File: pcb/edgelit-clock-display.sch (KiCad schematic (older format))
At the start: 42 parts, among them J1 Conn_01x03, J2 Conn_01x03

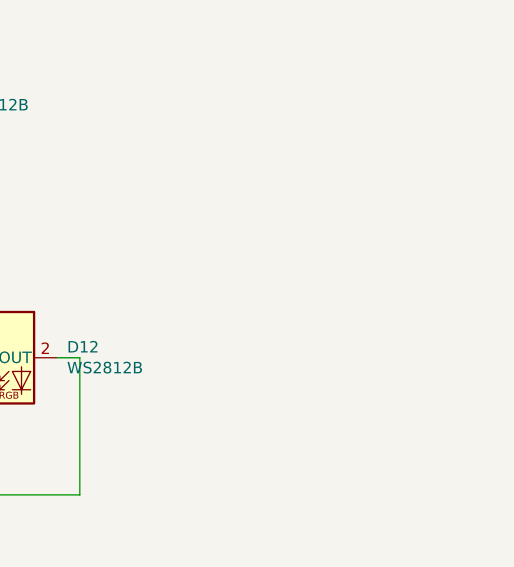
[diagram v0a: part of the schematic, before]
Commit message: Resized for a 30mm digit width, with 5mm between digits
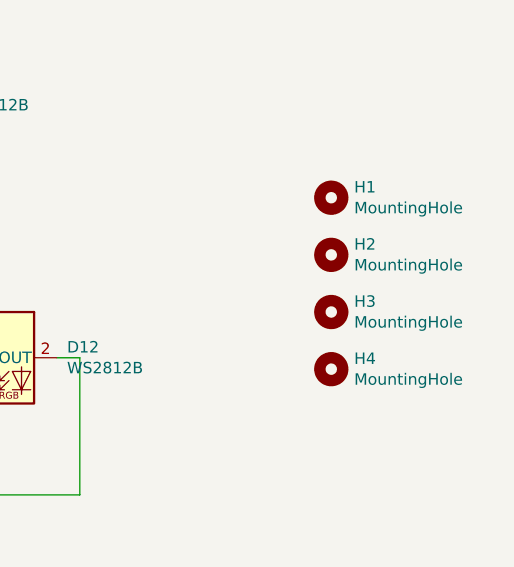
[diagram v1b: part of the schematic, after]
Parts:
- added H1, H2, H3, H4: MountingHole, Mounting_Holes:MountingHole_3.2mm_M3_DIN965, symbol Mechanical:MountingHole
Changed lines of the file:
@@
 	6650 12150 6000 12150
 Connection ~ 6000 12150
+$Comp
+L Mechanical:MountingHole H1
+U 1 1 6122DB00
+P 8000 3000
+F 0 "H1" H 8100 3046 50  0000 L CNN
+F 1 "MountingHole" H 8100 2955 50  0000 L CNN
+F 2 "Mounting_Holes:MountingHole_3.2mm_M3_DIN965" H 8000 3000 50  0001 C CNN
+F 3 "~" H 8000 3000 50  0001 C CNN
+	1    8000 3000
+	1    0    0    -1
+$EndComp
+$Comp
+L Mechanical:MountingHole H2
+U 1 1 6122DFBC
+P 8000 3250
+F 0 "H2" H 8100 3296 50  0000 L CNN
+F 1 "MountingHole" H 8100 3205 50  0000 L CNN
+F 2 "Mounting_Holes:MountingHole_3.2mm_M3_DIN965" H 8000 3250 50  0001 C CNN
+F 3 "~" H 8000 3250 50  0001 C CNN
+	1    8000 3250
+	1    0    0    -1
+$EndComp
+$Comp
+L Mechanical:MountingHole H3
+U 1 1 6122E128
+P 8000 3500
+F 0 "H3" H 8100 3546 50  0000 L CNN
+F 1 "MountingHole" H 8100 3455 50  0000 L CNN
+F 2 "Mounting_Holes:MountingHole_3.2mm_M3_DIN965" H 8000 3500 50  0001 C CNN
+F 3 "~" H 8000 3500 50  0001 C CNN
+	1    8000 3500
+	1    0    0    -1
+$EndComp
+$Comp
+L Mechanical:MountingHole H4
+U 1 1 6122E2C7
+P 8000 3750
+F 0 "H4" H 8100 3796 50  0000 L CNN
+F 1 "MountingHole" H 8100 3705 50  0000 L CNN
+F 2 "Mounting_Holes:MountingHole_3.2mm_M3_DIN965" H 8000 3750 50  0001 C CNN
+F 3 "~" H 8000 3750 50  0001 C CNN
+	1    8000 3750
+	1    0    0    -1
+$EndComp
 $EndSCHEMATC
